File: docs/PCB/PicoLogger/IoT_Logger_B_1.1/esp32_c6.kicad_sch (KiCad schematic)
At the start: 23 parts, among them J2 ESP_UART, Q1 BSS138, Q2 AO3407, SW1 Tact Switch 6x6mm / 13mm, SW2 Tact Switch 6x6mm / 13mm, U2 ESP32-C6-WROOM-1U

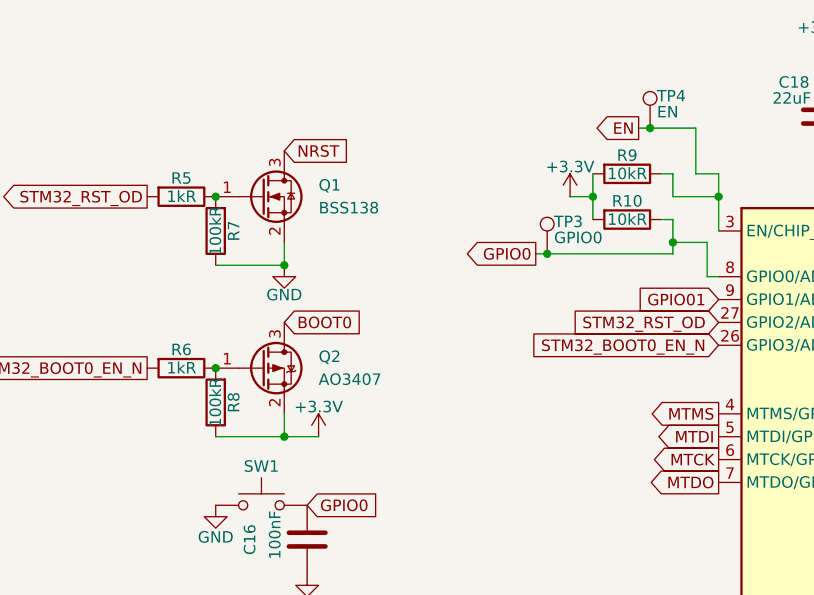
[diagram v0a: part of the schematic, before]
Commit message: New logger revisions added.
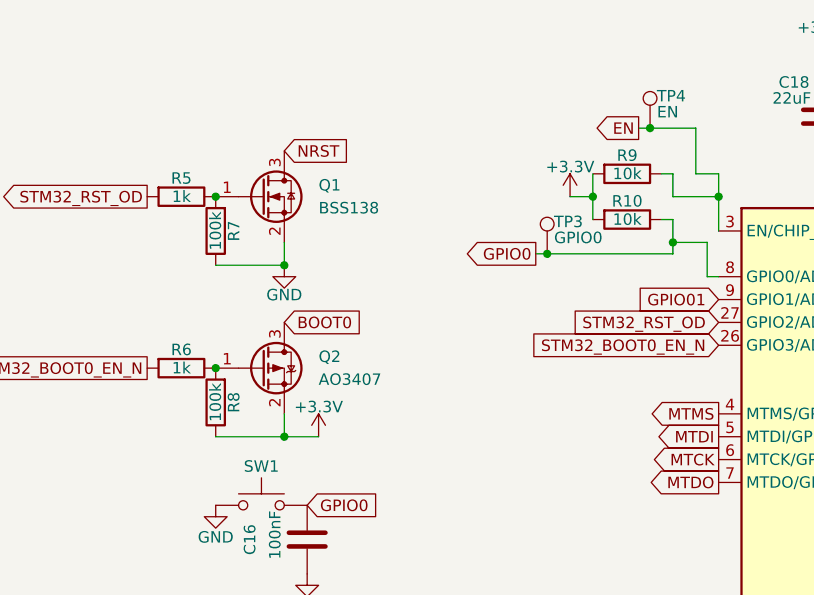
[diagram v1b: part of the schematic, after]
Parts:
- R10, R9: value 10kR -> 10k
- R5, R6: value 1kR -> 1k
- R7, R8: value 100kR -> 100k
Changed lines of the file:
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@@
 			)
 		)
-		(property "Value" "1kR"
+		(property "Value" "1k"
 			(at 68.58 69.85 90)
 			(effects
@@
 			)
 		)
-		(property "Value" "100kR"
+		(property "Value" "100k"
 			(at 72.39 73.66 90)
 			(effects
@@
 			)
 		)
-		(property "Value" "10kR"
+		(property "Value" "10k"
 			(at 118.11 67.31 90)
 			(effects
@@
 			)
 		)
-		(property "Value" "100kR"
+		(property "Value" "100k"
 			(at 72.39 92.71 90)
 			(effects
@@
 			)
 		)
-		(property "Value" "10kR"
+		(property "Value" "10k"
 			(at 118.11 72.39 90)
 			(effects
@@
 			)
 		)
-		(property "Value" "1kR"
+		(property "Value" "1k"
 			(at 68.58 88.9 90)
 			(effects
